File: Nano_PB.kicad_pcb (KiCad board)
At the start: 2 copper layers, 100 x 50 mm, 131 parts, among them CON1 BARREL_JACK, P1 CONN_02X04, P10 CONN_01X04, P11 CONN_01X04, P12 CONN_01X04, P13 CONN_01X01, P14 CONN_01X01, P15 CONN_01X01, P16 CONN_01X01, P17 CONN_01X01, P2 CONN_01X06, P3 CONN_01X01, P4 CONN_01X03, P5 CONN_01X03, P6 CONN_01X03, P7 CONN_01X03, P8 CONN_01X03, P9 CONN_01X04, Q1 SMBT3904, Q2 SMBT3904, Q3 SMBT3904, Q4 SMBT3904, Q5 SMBT3904, Q6 BSS138, Q7 BSS138, Q8 SMBT3904, Q9 SMBT3904, SW1 Izquierda, SW2 Arriba, SW3 Abajo, SW4 Derecha, U1 Arduino_Nano, U2 LM7805CT, U3 MCP23017, U5 Matriz_5x7, U6 PCA9551, U8 MMA7660FC, U9 40106

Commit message: finalizado enrutado provisional
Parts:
- removed C10, C11, C8, C9: 1u, Capacitors_SMD:C_0805
- removed the Gnd-Via at (121.5, 65.0)
- removed the Gnd-Via at (140.4, 25.4)
- added Gnd-Via: VAL**, Vias:Gnd-Via, F.Cu at (53.5, 37.1)
- added Gnd-Via: VAL**, Vias:Gnd-Via, B.Cu at (116.7, 61.4)
- added Gnd-Via: VAL**, Vias:Gnd-Via, B.Cu at (108.4, 60.1)
- added Gnd-Via: VAL**, Vias:Gnd-Via, B.Cu at (108.7, 57.2)
- C17, C19: moved to B.Cu
- moved G*** 14.5 mm to (117.4, 49.4)
- moved R24 9.48 mm to (84.2, 56.6)
- moved R27 7.92 mm to (84.2, 65.0)
- moved R25 3.68 mm to (84.2, 59.4)
- moved C20 2.95 mm to (144.6, 65.2), turned to 180 degrees
- moved R26 2.12 mm to (84.2, 62.2)
- moved R50 1.55 mm to (72.7, 46.0)
- moved R45 1.41 mm to (144.6, 58.9)
- moved R36 1.28 mm to (78.1, 45.9)
- moved C15 1.25 mm to (74.5, 61.1)
- moved C16 1.25 mm to (79.0, 61.1)
- moved SP1 1.11 mm to (78.0, 53.7)
- moved Gnd-Via 1.07 mm to (137.9, 34.0)
- moved Gnd-Via 1.07 mm to (137.9, 30.7)
- moved Gnd-Via 1.07 mm to (137.9, 27.3)
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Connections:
- C15 pad 1: D2 -> D5
- C16 pad 1: D5 -> D2
- R10 pad 2: PB1 -> PB5
- R11 pad 2: PB2 -> PB6
- R12 pad 2: PB3 -> PB7
- R24 pad 2: PB4 -> PB3
- R25 pad 2: PB5 -> PB2
- R26 pad 2: PB6 -> PB1
- R27 pad 2: PB7 -> PB0
- R40 pad 2: D2 -> D5
- R42 pad 2: D5 -> D2
- R9 pad 2: PB0 -> PB4
- SW1 pad 2: PB5 -> PB2
- SW2 pad 2: PB4 -> PB3
- SW3 pad 2: PB7 -> PB0
- SW4 pad 2: PB6 -> PB1
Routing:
- net +5V: track 252.0 -> 434.1 mm, vias 0 -> 9
- net A7: track 0.00 -> 99.3 mm
- net ~RESET: track 0.00 -> 91.6 mm, vias 0 -> 5
- net BUZZER: track 0.00 -> 67.5 mm, vias 0 -> 3
- net A2: track 3.57 -> 69.6 mm, vias 0 -> 1
- net D3: track 0.00 -> 61.7 mm, vias 0 -> 2
- net A1: track 4.17 -> 63.0 mm, vias 0 -> 1
- net A5: track 32.9 -> 89.6 mm, vias 0 -> 3
- net A0: track 3.57 -> 55.3 mm, vias 0 -> 1
- net A4: track 43.3 -> 92.1 mm, vias 0 -> 5
- net A3: track 30.2 -> 78.0 mm, vias 0 -> 1
- net D2: track 0.00 -> 45.4 mm
- net D12: track 48.0 -> 91.2 mm
- net D5: track 0.00 -> 40.1 mm
- net PB7: track 0.00 -> 39.2 mm, vias 0 -> 2
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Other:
- board text removed: "Key"

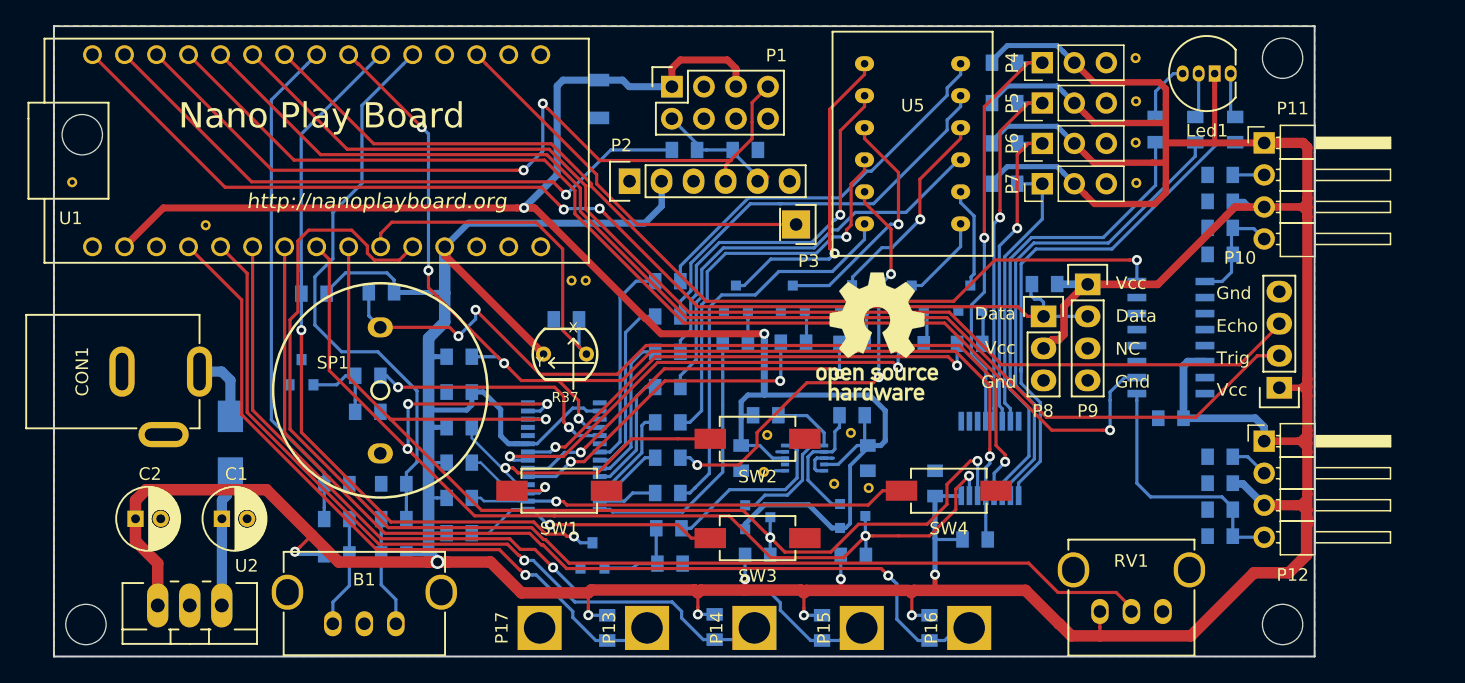
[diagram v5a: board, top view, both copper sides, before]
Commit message: ordenar trazado, añadir vias de union de planos gnd
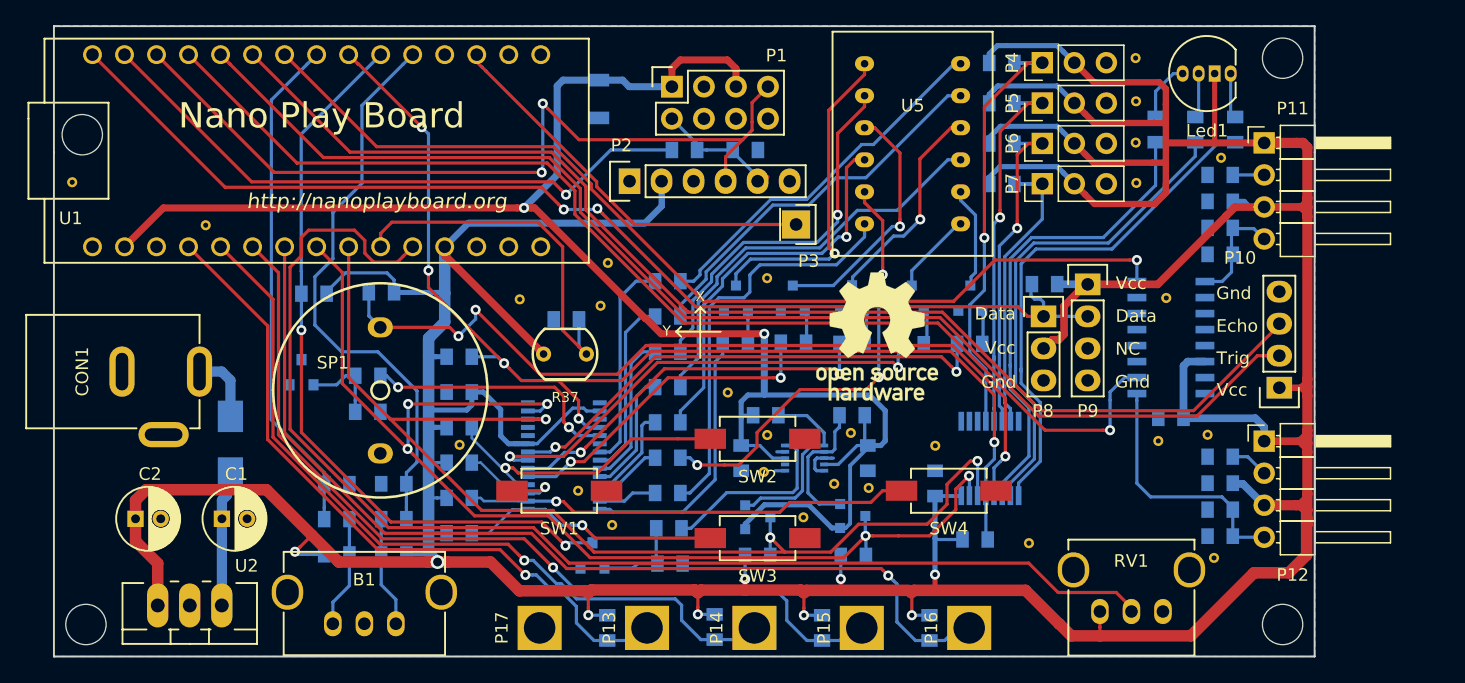
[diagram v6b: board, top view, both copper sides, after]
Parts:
- added Gnd-Via: VAL**, Vias:Gnd-Via, F.Cu at (144.7, 35.2)
- added Gnd-Via: VAL**, Vias:Gnd-Via, F.Cu at (84.3, 58.0)
- added Gnd-Via: VAL**, Vias:Gnd-Via, F.Cu at (96.0, 43.5)
- added Gnd-Via: VAL**, Vias:Gnd-Via, F.Cu at (105.5, 53.8)
- added Gnd-Via: VAL**, Vias:Gnd-Via, F.Cu at (108.7, 44.8)
- added Gnd-Via: VAL**, Vias:Gnd-Via, B.Cu at (111.5, 63.7)
- added Gnd-Via: VAL**, Vias:Gnd-Via, F.Cu at (140.3, 46.3)
- added Gnd-Via: VAL**, Vias:Gnd-Via, F.Cu at (144.1, 67.0)
- added Gnd-Via: VAL**, Vias:Gnd-Via, F.Cu at (143.6, 57.2)
- added Gnd-Via: VAL**, Vias:Gnd-Via, F.Cu at (139.7, 57.7)
- added Gnd-Via: VAL**, Vias:Gnd-Via, F.Cu at (122.0, 58.0)
- added Gnd-Via: VAL**, Vias:Gnd-Via, F.Cu at (129.4, 65.8)
- added Gnd-Via: VAL**, Vias:Gnd-Via, F.Cu at (96.4, 64.3)
- added Gnd-Via: VAL**, Vias:Gnd-Via, F.Cu at (93.7, 61.6)
- moved Gnd-Via 4.37 mm to (89.0, 46.4)
- moved Gnd-Via 2.32 mm to (95.5, 47.0)
- moved R18 0.22 mm to (127.3, 34.1)
- moved R16 0.22 mm to (127.3, 27.7)
- moved R17 0.22 mm to (127.3, 30.9)
- moved R19 0.22 mm to (127.3, 37.3)
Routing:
- net D7: track 94.2 -> 97.2 mm
- net +5V: track 434.1 -> 436.7 mm
- net SERVO1: track 33.9 -> 36.2 mm
- net Net-(R2-Pad1): track 32.8 -> 30.5 mm
- net SERVO3: track 26.2 -> 28.4 mm
- net SERVO2: track 29.7 -> 32.0 mm
- net SERVO4: track 22.2 -> 24.5 mm
- net A5: track 89.6 -> 91.2 mm
- net Net-(R1-Pad1): track 31.1 -> 29.7 mm
- net D10: track 64.8 -> 66.0 mm
- net Net-(R4-Pad1): track 34.2 -> 33.1 mm
- net Net-(R5-Pad1): track 32.2 -> 31.2 mm
- net Net-(R3-Pad1): track 30.7 -> 29.8 mm
- net Net-(Q2-Pad3): track 19.1 -> 19.9 mm
- net Net-(R7-Pad1): track 32.3 -> 32.9 mm
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
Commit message: Modificaciones menores en serigrafia
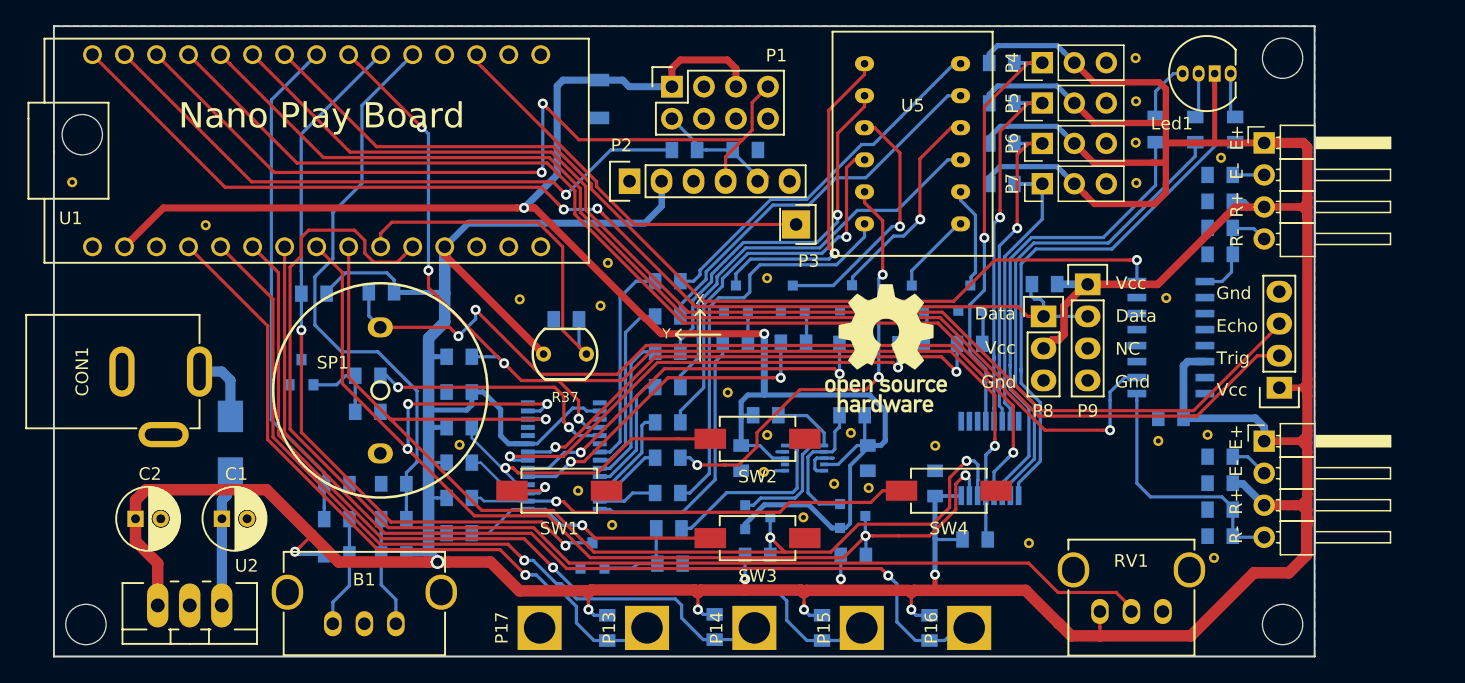
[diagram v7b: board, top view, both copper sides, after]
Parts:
- moved G*** 1.17 mm to (118.1, 50.3)
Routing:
- net +5V: track 436.7 -> 438.2 mm
- net BUZZER: track 67.2 -> 67.7 mm

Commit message: Revisado V0.4. Actualizados gerber y esquemas
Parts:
- moved C5 1.30 mm to (94.1, 30.9)
- moved P1 0.79 mm to (100.3, 29.6)
- moved Gnd-Via 0.07 mm to (96.0, 43.5)
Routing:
- net D5: track 40.1 -> 46.8 mm
- net D7: track 97.2 -> 100.0 mm
- net D2: track 45.4 -> 46.8 mm
- net D10: track 66.0 -> 67.3 mm
- net D8: track 99.0 -> 100.0 mm
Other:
- board text added: "A0"
- board text added: "A1"
- board text added: "A2"
- board text added: "A3"
- board text added: "DTH11"
- board text added: "ESP8266"
- board text added: "GND"
- board text added: "HC-05/06"
- board text added: "HC-SR04"
- board text added: "SERVO"
